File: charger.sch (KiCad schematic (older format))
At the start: 22 parts, among them IC1 BQ51050B

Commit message: Added resistor and capacitor values, footprints and NPNs
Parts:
- C14: footprint (none) -> Capacitors_SMD:C_0402; MPN (none) -> GCM155R71E103KA37D
- C15: footprint (none) -> Capacitors_SMD:C_0402; MPN (none) -> GCM155R71H223KA55D
- C16: footprint (none) -> Capacitors_SMD:C_0402; MPN (none) -> GRT155R61E474KE01D
- C17, C18, C19, C22, C23: footprint (none) -> Capacitors_SMD:C_0402
- C20: footprint (none) -> Capacitors_SMD:C_0603; MPN (none) -> CC0603KRX5R7BB475
- C21: footprint (none) -> Capacitors_SMD:C_0603
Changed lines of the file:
@@
 Battery_voltage
 $Comp
-L +BATT #PWR50
+L +BATT #PWR040
 U 1 1 5AA78F36
 P 8450 2600
-F 0 "#PWR50" H 8450 2450 50  0001 C CNN
+F 0 "#PWR040" H 8450 2450 50  0001 C CNN
 F 1 "+BATT" H 8450 2740 50  0000 C CNN
 F 2 "" H 8450 2600 50  0001 C CNN
@@
 $EndComp
 $Comp
-L GND #PWR51
+L GND #PWR041
 U 1 1 5AA78FC5
 P 8450 3400
-F 0 "#PWR51" H 8450 3150 50  0001 C CNN
+F 0 "#PWR041" H 8450 3150 50  0001 C CNN
 F 1 "GND" H 8450 3250 50  0000 C CNN
 F 2 "" H 8450 3400 50  0001 C CNN
@@
 $EndComp
 $Comp
-L GND #PWR40
+L GND #PWR042
 U 1 1 5AA85C8F
 P 4750 4600
-F 0 "#PWR40" H 4750 4350 50  0001 C CNN
+F 0 "#PWR042" H 4750 4350 50  0001 C CNN
 F 1 "GND" H 4750 4450 50  0000 C CNN
 F 2 "" H 4750 4600 50  0001 C CNN
@@
 $EndComp
 $Comp
-L +BATT #PWR42
+L +BATT #PWR043
 U 1 1 5AA85D44
 P 5100 2800
-F 0 "#PWR42" H 5100 2650 50  0001 C CNN
+F 0 "#PWR043" H 5100 2650 50  0001 C CNN
 F 1 "+BATT" H 5100 2940 50  0000 C CNN
 F 2 "" H 5100 2800 50  0001 C CNN
@@
 $EndComp
 $Comp
-L GND #PWR41
+L GND #PWR044
 U 1 1 5AA86D68
 P 4950 4600
-F 0 "#PWR41" H 4950 4350 50  0001 C CNN
+F 0 "#PWR044" H 4950 4350 50  0001 C CNN
 F 1 "GND" H 4950 4450 50  0000 C CNN
 F 2 "" H 4950 4600 50  0001 C CNN
@@
 $EndComp
 $Comp
-L +BATT #PWR48
+L +BATT #PWR045
 U 1 1 5AA87B72
 P 8450 1150
-F 0 "#PWR48" H 8450 1000 50  0001 C CNN
+F 0 "#PWR045" H 8450 1000 50  0001 C CNN
 F 1 "+BATT" H 8450 1290 50  0000 C CNN
 F 2 "" H 8450 1150 50  0001 C CNN
@@
 F 0 "C23" H 8475 1500 50  0000 L CNN
 F 1 "2u2 6V3" V 8300 1250 50  0000 L CNN
-F 2 "" H 8488 1250 50  0001 C CNN
+F 2 "Capacitors_SMD:C_0402" H 8488 1250 50  0001 C CNN
 F 3 "" H 8450 1400 50  0001 C CNN
 	1    8450 1400
@@
 $EndComp
 $Comp
-L GND #PWR49
+L GND #PWR046
 U 1 1 5AA87C01
 P 8450 1650
-F 0 "#PWR49" H 8450 1400 50  0001 C CNN
+F 0 "#PWR046" H 8450 1400 50  0001 C CNN
 F 1 "GND" H 8450 1500 50  0000 C CNN
 F 2 "" H 8450 1650 50  0001 C CNN
@@
 F 0 "C14" V 3250 2850 50  0000 L CNN
 F 1 "10nF 10V" V 3250 2400 50  0000 L CNN
-F 2 "" H 3188 2650 50  0001 C CNN
+F 2 "Capacitors_SMD:C_0402" H 3188 2650 50  0001 C CNN
 F 3 "" H 3150 2800 50  0001 C CNN
+F 4 "GCM155R71E103KA37D" V 3150 2800 60  0001 C CNN "MPN"
 	1    3150 2800
 	0    -1   -1   0
@@
 F 0 "C19" V 3250 4300 50  0000 L CNN
 F 1 "10nF 10V" V 3250 4550 50  0000 L CNN
-F 2 "" H 3188 4350 50  0001 C CNN
+F 2 "Capacitors_SMD:C_0402" H 3188 4350 50  0001 C CNN
 F 3 "" H 3150 4500 50  0001 C CNN
 	1    3150 4500
@@
 F 0 "C18" V 3250 4050 50  0000 L CNN
 F 1 "22nF 25V" V 3250 4300 50  0000 L CNN
-F 2 "" H 3188 4100 50  0001 C CNN
+F 2 "Capacitors_SMD:C_0402" H 3188 4100 50  0001 C CNN
 F 3 "" H 3150 4250 50  0001 C CNN
 	1    3150 4250
@@
 F 0 "C17" V 3250 3800 50  0000 L CNN
 F 1 "470nF 25V" V 3250 4050 50  0000 L CNN
-F 2 "" H 3188 3850 50  0001 C CNN
+F 2 "Capacitors_SMD:C_0402" H 3188 3850 50  0001 C CNN
 F 3 "" H 3150 4000 50  0001 C CNN
 	1    3150 4000
@@
 F 0 "C16" V 3050 3100 50  0000 L CNN
 F 1 "470nF 25V" V 3050 3350 50  0000 L CNN
-F 2 "" H 3188 3150 50  0001 C CNN
+F 2 "Capacitors_SMD:C_0402" H 3188 3150 50  0001 C CNN
 F 3 "" H 3150 3300 50  0001 C CNN
+F 4 "GRT155R61E474KE01D" V 3150 3300 60  0001 C CNN "MPN"
 	1    3150 3300
 	0    1    1    0
@@
 F 0 "C15" V 3250 3100 50  0000 L CNN
 F 1 "22nF 25V" V 3250 2650 50  0000 L CNN
-F 2 "" H 3188 2900 50  0001 C CNN
+F 2 "Capacitors_SMD:C_0402" H 3188 2900 50  0001 C CNN
 F 3 "" H 3150 3050 50  0001 C CNN
+F 4 "GCM155R71H223KA55D" V 3150 3050 60  0001 C CNN "MPN"
 	1    3150 3050
 	0    -1   -1   0
@@
 Connection ~ 2900 3300
 $Comp
-L VDD #PWR45
+L VDD #PWR047
 U 1 1 5AA8B638
 P 7050 2650
-F 0 "#PWR45" H 7050 2500 50  0001 C CNN
+F 0 "#PWR047" H 7050 2500 50  0001 C CNN
 F 1 "VDD" H 7050 2800 50  0000 C CNN
 F 2 "" H 7050 2650 50  0001 C CNN
@@
 $EndComp
 $Comp
-L GND #PWR46
+L GND #PWR048
 U 1 1 5AB06991
 P 7050 4600
-F 0 "#PWR46" H 7050 4350 50  0001 C CNN
+F 0 "#PWR048" H 7050 4350 50  0001 C CNN
 F 1 "GND" H 7050 4450 50  0000 C CNN
 F 2 "" H 7050 4600 50  0001 C CNN
@@
 F 0 "C20" H 5225 4350 50  0000 L CNN
 F 1 "4u7 16V" V 5400 4100 50  0000 L CNN
-F 2 "" H 5238 4100 50  0001 C CNN
+F 2 "Capacitors_SMD:C_0603" H 5238 4100 50  0001 C CNN
 F 3 "" H 5200 4250 50  0001 C CNN
+F 4 "CC0603KRX5R7BB475" H 5200 4250 60  0001 C CNN "MPN"
 	1    5200 4250
 	1    0    0    -1
@@
 	4650 3600 5550 3600
 $Comp
-L GND #PWR43
+L GND #PWR049
 U 1 1 5AB07537
 P 5200 4600
-F 0 "#PWR43" H 5200 4350 50  0001 C CNN
+F 0 "#PWR049" H 5200 4350 50  0001 C CNN
 F 1 "GND" H 5200 4450 50  0000 C CNN
 F 2 "" H 5200 4600 50  0001 C CNN
@@
 F 0 "C21" H 5575 4350 50  0000 L CNN
 F 1 "4u7 16V" V 5750 4100 50  0000 L CNN
-F 2 "" H 5588 4100 50  0001 C CNN
+F 2 "Capacitors_SMD:C_0603" H 5588 4100 50  0001 C CNN
 F 3 "" H 5550 4250 50  0001 C CNN
 	1    5550 4250
@@
 Connection ~ 5200 3600
 $Comp
-L GND #PWR44
+L GND #PWR050
 U 1 1 5AB15630
 P 5550 4600
-F 0 "#PWR44" H 5550 4350 50  0001 C CNN
+F 0 "#PWR050" H 5550 4350 50  0001 C CNN
 F 1 "GND" H 5550 4450 50  0000 C CNN
 F 2 "" H 5550 4600 50  0001 C CNN
@@
 F 0 "C22" H 7125 1450 50  0000 L CNN
 F 1 "470nF 25V" H 7125 1250 50  0000 L CNN
-F 2 "" H 7138 1200 50  0001 C CNN
+F 2 "Capacitors_SMD:C_0402" H 7138 1200 50  0001 C CNN
 F 3 "" H 7100 1350 50  0001 C CNN
 	1    7100 1350
@@
 $EndComp
 $Comp
-L GND #PWR47
+L GND #PWR051
 U 1 1 5AB160F7
 P 7100 1650
-F 0 "#PWR47" H 7100 1400 50  0001 C CNN
+F 0 "#PWR051" H 7100 1400 50  0001 C CNN
 F 1 "GND" H 7100 1500 50  0000 C CNN
 F 2 "" H 7100 1650 50  0001 C CNN
@@
 	7050 3800 7050 3850
 $Comp
-L PWR_FLAG #FLG1
+L PWR_FLAG #FLG052
 U 1 1 5AB77961
 P 2500 3350
-F 0 "#FLG1" H 2500 3425 50  0001 C CNN
+F 0 "#FLG052" H 2500 3425 50  0001 C CNN
 F 1 "PWR_FLAG" H 2500 3500 50  0000 C CNN
 F 2 "" H 2500 3350 50  0001 C CNN
@@
 $EndComp
 $Comp
-L PWR_FLAG #FLG2
+L PWR_FLAG #FLG053
 U 1 1 5AB77A5F
 P 2900 3700
-F 0 "#FLG2" H 2900 3775 50  0001 C CNN
+F 0 "#FLG053" H 2900 3775 50  0001 C CNN
 F 1 "PWR_FLAG" H 2900 3850 50  0000 C CNN
 F 2 "" H 2900 3700 50  0001 C CNN

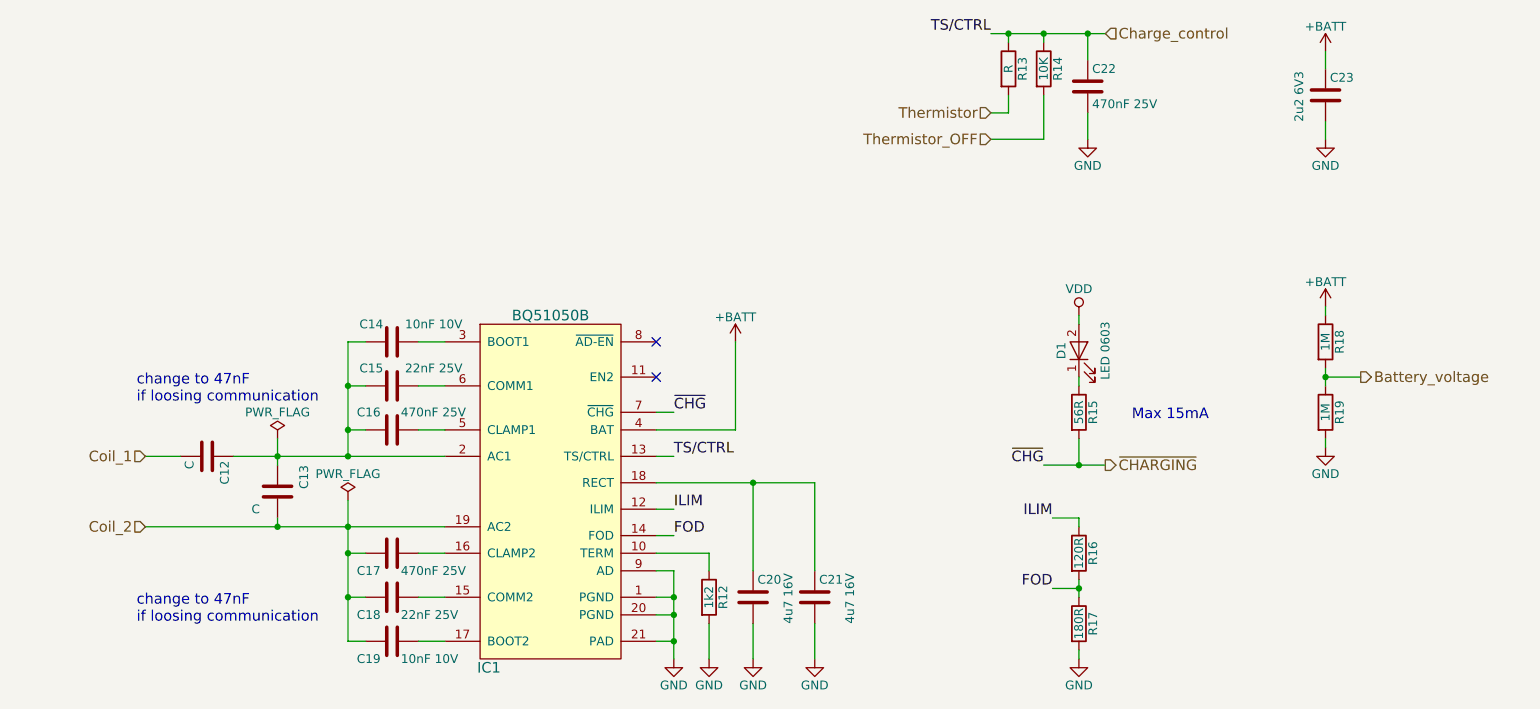
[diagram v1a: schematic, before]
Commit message: Removed boost converter, added output switch
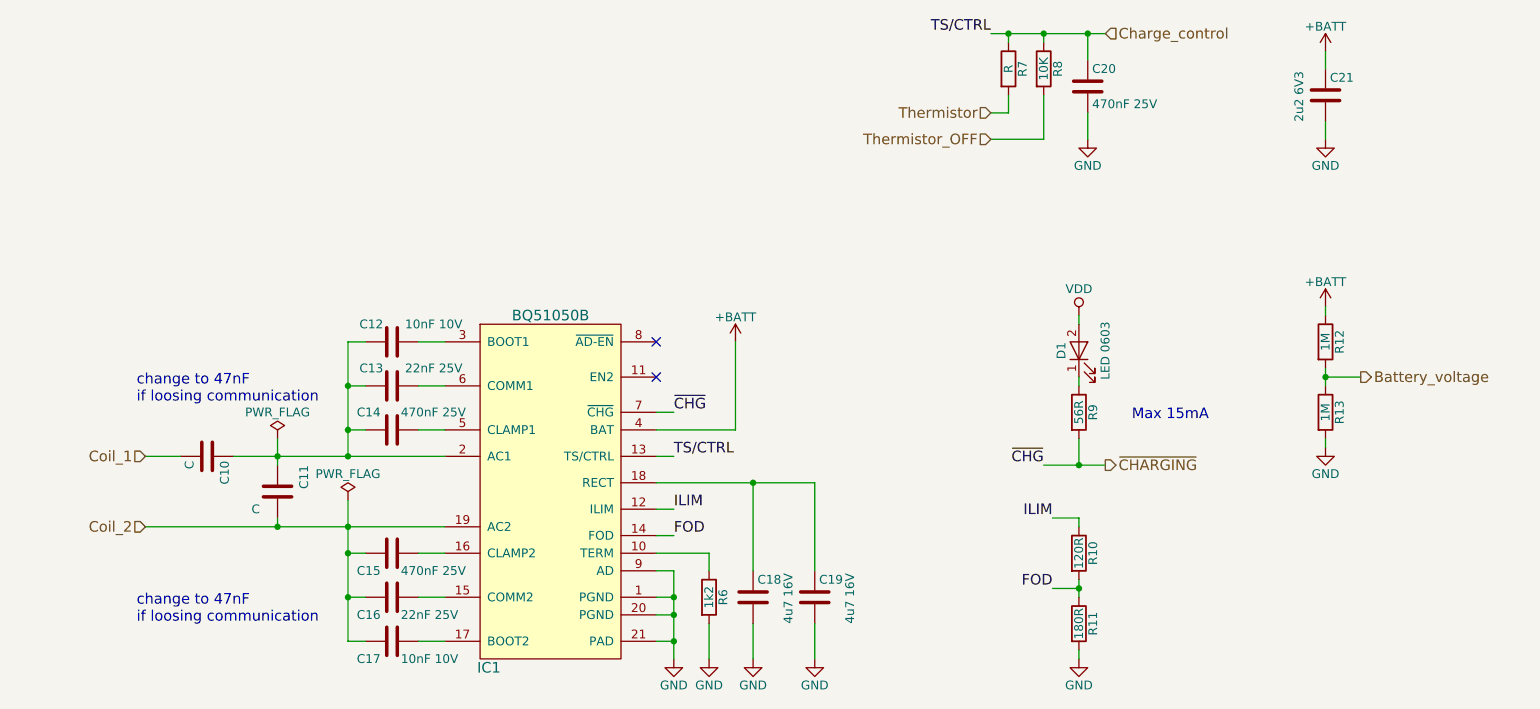
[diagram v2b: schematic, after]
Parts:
- renumbered C12 to C10, C13 to C11, C14 to C12, C15 to C13, C16 to C14, C17 to C15, C18 to C16, C19 to C17, C20 to C18, C21 to C19, C22 to C20, C23 to C21, R16 to R10, R17 to R11, R18 to R12, R19 to R13, R12 to R6, R13 to R7, R14 to R8, R15 to R9
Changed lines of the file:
@@
 LIBS:Transistor
 LIBS:Connector
+LIBS:lakotamm-loadswitch
 LIBS:F3K_Battery_manager-cache
 EELAYER 25 0
@@
 $Descr A4 11693 8268
 encoding utf-8
-Sheet 4 4
+Sheet 3 3
 Title ""
 Date ""
@@
 Battery_voltage
 $Comp
-L +BATT #PWR040
+L +BATT #PWR47
 U 1 1 5AA78F36
 P 8450 2600
-F 0 "#PWR040" H 8450 2450 50  0001 C CNN
+F 0 "#PWR47" H 8450 2450 50  0001 C CNN
 F 1 "+BATT" H 8450 2740 50  0000 C CNN
 F 2 "" H 8450 2600 50  0001 C CNN
@@
 $EndComp
 $Comp
-L R R18
+L R R12
 U 1 1 5AA78F4C
 P 8450 2800
-F 0 "R18" V 8530 2800 50  0000 C CNN
+F 0 "R12" V 8530 2800 50  0000 C CNN
 F 1 "1M" V 8450 2800 50  0000 C CNN
 F 2 "Resistors_SMD:R_0402" V 8380 2800 50  0001 C CNN
@@
 $EndComp
 $Comp
-L R R19
+L R R13
 U 1 1 5AA78F86
 P 8450 3200
-F 0 "R19" V 8530 3200 50  0000 C CNN
+F 0 "R13" V 8530 3200 50  0000 C CNN
 F 1 "1M" V 8450 3200 50  0000 C CNN
 F 2 "Resistors_SMD:R_0402" V 8380 3200 50  0001 C CNN
@@
 $EndComp
 $Comp
-L GND #PWR041
+L GND #PWR48
 U 1 1 5AA78FC5
 P 8450 3400
-F 0 "#PWR041" H 8450 3150 50  0001 C CNN
+F 0 "#PWR48" H 8450 3150 50  0001 C CNN
 F 1 "GND" H 8450 3250 50  0000 C CNN
 F 2 "" H 8450 3400 50  0001 C CNN
@@
 $EndComp
 $Comp
-L GND #PWR042
+L GND #PWR37
 U 1 1 5AA85C8F
 P 4750 4600
-F 0 "#PWR042" H 4750 4350 50  0001 C CNN
+F 0 "#PWR37" H 4750 4350 50  0001 C CNN
 F 1 "GND" H 4750 4450 50  0000 C CNN
 F 2 "" H 4750 4600 50  0001 C CNN
@@
 $EndComp
 $Comp
-L +BATT #PWR043
+L +BATT #PWR39
 U 1 1 5AA85D44
 P 5100 2800
-F 0 "#PWR043" H 5100 2650 50  0001 C CNN
+F 0 "#PWR39" H 5100 2650 50  0001 C CNN
 F 1 "+BATT" H 5100 2940 50  0000 C CNN
 F 2 "" H 5100 2800 50  0001 C CNN
@@
 NoConn ~ 4650 2800
 $Comp
-L R R15
+L R R9
 U 1 1 5AA85E7B
 P 7050 3200
-F 0 "R15" V 7130 3200 50  0000 C CNN
+F 0 "R9" V 7130 3200 50  0000 C CNN
 F 1 "56R" V 7050 3200 50  0000 C CNN
 F 2 "Resistors_SMD:R_0402" V 6980 3200 50  0001 C CNN
@@
 ~CHARGING
 $Comp
-L R R12
+L R R6
 U 1 1 5AA86C77
 P 4950 4250
-F 0 "R12" V 5030 4250 50  0000 C CNN
+F 0 "R6" V 5030 4250 50  0000 C CNN
 F 1 "1k2" V 4950 4250 50  0000 C CNN
 F 2 "Resistors_SMD:R_0402" V 4880 4250 50  0001 C CNN
@@
 $EndComp
 $Comp
-L GND #PWR044
+L GND #PWR38
 U 1 1 5AA86D68
 P 4950 4600
-F 0 "#PWR044" H 4950 4350 50  0001 C CNN
+F 0 "#PWR38" H 4950 4350 50  0001 C CNN
 F 1 "GND" H 4950 4450 50  0000 C CNN
 F 2 "" H 4950 4600 50  0001 C CNN
@@
 $EndComp
 $Comp
-L +BATT #PWR045
+L +BATT #PWR45
 U 1 1 5AA87B72
 P 8450 1150
-F 0 "#PWR045" H 8450 1000 50  0001 C CNN
+F 0 "#PWR45" H 8450 1000 50  0001 C CNN
 F 1 "+BATT" H 8450 1290 50  0000 C CNN
 F 2 "" H 8450 1150 50  0001 C CNN
@@
 $EndComp
 $Comp
-L C C23
+L C C21
 U 1 1 5AA87B8B
 P 8450 1400
-F 0 "C23" H 8475 1500 50  0000 L CNN
+F 0 "C21" H 8475 1500 50  0000 L CNN
 F 1 "2u2 6V3" V 8300 1250 50  0000 L CNN
 F 2 "Capacitors_SMD:C_0402" H 8488 1250 50  0001 C CNN
@@
 $EndComp
 $Comp
-L GND #PWR046
+L GND #PWR46
 U 1 1 5AA87C01
 P 8450 1650
-F 0 "#PWR046" H 8450 1400 50  0001 C CNN
+F 0 "#PWR46" H 8450 1400 50  0001 C CNN
 F 1 "GND" H 8450 1500 50  0000 C CNN
 F 2 "" H 8450 1650 50  0001 C CNN
@@
 $EndComp
 $Comp
-L C C14
+L C C12
 U 1 1 5AA87D3B
 P 3150 2800
-F 0 "C14" V 3250 2850 50  0000 L CNN
+F 0 "C12" V 3250 2850 50  0000 L CNN
 F 1 "10nF 10V" V 3250 2400 50  0000 L CNN
 F 2 "Capacitors_SMD:C_0402" H 3188 2650 50  0001 C CNN
@@
 $EndComp
 $Comp
-L C C19
+L C C17
 U 1 1 5AA87DF5
 P 3150 4500
-F 0 "C19" V 3250 4300 50  0000 L CNN
+F 0 "C17" V 3250 4300 50  0000 L CNN
 F 1 "10nF 10V" V 3250 4550 50  0000 L CNN
 F 2 "Capacitors_SMD:C_0402" H 3188 4350 50  0001 C CNN
@@
 $EndComp
 $Comp
-L C C18
+L C C16
 U 1 1 5AA882B8
 P 3150 4250
-F 0 "C18" V 3250 4050 50  0000 L CNN
+F 0 "C16" V 3250 4050 50  0000 L CNN
 F 1 "22nF 25V" V 3250 4300 50  0000 L CNN
 F 2 "Capacitors_SMD:C_0402" H 3188 4100 50  0001 C CNN
@@
 change to 47nF \nif loosing communication
 $Comp
-L C C17
+L C C15
 U 1 1 5AA8A27D
 P 3150 4000
-F 0 "C17" V 3250 3800 50  0000 L CNN
+F 0 "C15" V 3250 3800 50  0000 L CNN
 F 1 "470nF 25V" V 3250 4050 50  0000 L CNN
 F 2 "Capacitors_SMD:C_0402" H 3188 3850 50  0001 C CNN
@@
 $EndComp
 $Comp
-L C C16
+L C C14
 U 1 1 5AA8A4C2
 P 3150 3300
-F 0 "C16" V 3050 3100 50  0000 L CNN
+F 0 "C14" V 3050 3100 50  0000 L CNN
 F 1 "470nF 25V" V 3050 3350 50  0000 L CNN
 F 2 "Capacitors_SMD:C_0402" H 3188 3150 50  0001 C CNN
@@
 $EndComp
 $Comp
-L C C15
+L C C13
 U 1 1 5AA88198
 P 3150 3050
-F 0 "C15" V 3250 3100 50  0000 L CNN
+F 0 "C13" V 3250 3100 50  0000 L CNN
 F 1 "22nF 25V" V 3250 2650 50  0000 L CNN
 F 2 "Capacitors_SMD:C_0402" H 3188 2900 50  0001 C CNN
@@
 Connection ~ 2900 3300
 $Comp
-L VDD #PWR047
+L VDD #PWR42
 U 1 1 5AA8B638
 P 7050 2650
-F 0 "#PWR047" H 7050 2500 50  0001 C CNN
+F 0 "#PWR42" H 7050 2500 50  0001 C CNN
 F 1 "VDD" H 7050 2800 50  0000 C CNN
 F 2 "" H 7050 2650 50  0001 C CNN
@@
 Max 15mA\n
 $Comp
-L C C13
+L C C11
 U 1 1 5AB055C0
 P 2500 3650
-F 0 "C13" V 2350 3500 50  0000 L CNN
+F 0 "C11" V 2350 3500 50  0000 L CNN
 F 1 "C" H 2600 3750 50  0000 L CNN
 F 2 "" H 2538 3500 50  0001 C CNN
@@
 $EndComp
 $Comp
-L C C12
+L C C10
 U 1 1 5AB0567E
 P 2100 3450
-F 0 "C12" H 2125 3550 50  0000 L CNN
+F 0 "C10" H 2125 3550 50  0000 L CNN
 F 1 "C" H 2125 3350 50  0000 L CNN
 F 2 "" H 2138 3300 50  0001 C CNN
@@
 	2900 3700 2900 4500
 $Comp
-L R R17
+L R R11
 U 1 1 5AB0687F
 P 7050 4400
-F 0 "R17" V 7130 4400 50  0000 C CNN
+F 0 "R11" V 7130 4400 50  0000 C CNN
 F 1 "180R" V 7050 4400 50  0000 C CNN
 F 2 "Resistors_SMD:R_0402" V 6980 4400 50  0001 C CNN
@@
 $EndComp
 $Comp
-L GND #PWR048
+L GND #PWR43
 U 1 1 5AB06991
 P 7050 4600
-F 0 "#PWR048" H 7050 4350 50  0001 C CNN
+F 0 "#PWR43" H 7050 4350 50  0001 C CNN
 F 1 "GND" H 7050 4450 50  0000 C CNN
 F 2 "" H 7050 4600 50  0001 C CNN
@@
 	4650 3450 4750 3450
 $Comp
-L C C20
+L C C18
 U 1 1 5AB0745B
 P 5200 4250
-F 0 "C20" H 5225 4350 50  0000 L CNN
+F 0 "C18" H 5225 4350 50  0000 L CNN
 F 1 "4u7 16V" V 5400 4100 50  0000 L CNN
 F 2 "Capacitors_SMD:C_0603" H 5238 4100 50  0001 C CNN
@@
 	4650 3600 5550 3600
 $Comp
-L GND #PWR049
+L GND #PWR40
 U 1 1 5AB07537
 P 5200 4600
-F 0 "#PWR049" H 5200 4350 50  0001 C CNN
+F 0 "#PWR40" H 5200 4350 50  0001 C CNN
 F 1 "GND" H 5200 4450 50  0000 C CNN
 F 2 "" H 5200 4600 50  0001 C CNN
@@
 Thermistor
 $Comp
-L C C21
+L C C19
 U 1 1 5AB15596
 P 5550 4250
-F 0 "C21" H 5575 4350 50  0000 L CNN
+F 0 "C19" H 5575 4350 50  0000 L CNN
 F 1 "4u7 16V" V 5750 4100 50  0000 L CNN
 F 2 "Capacitors_SMD:C_0603" H 5588 4100 50  0001 C CNN
@@
 Connection ~ 5200 3600
 $Comp
-L GND #PWR050
+L GND #PWR41
 U 1 1 5AB15630
 P 5550 4600
-F 0 "#PWR050" H 5550 4350 50  0001 C CNN
+F 0 "#PWR41" H 5550 4350 50  0001 C CNN
 F 1 "GND" H 5550 4450 50  0000 C CNN
 F 2 "" H 5550 4600 50  0001 C CNN
@@
 	5550 4400 5550 4600
 $Comp
-L R R13
+L R R7
 U 1 1 5AB15ADC
 P 6650 1250
-F 0 "R13" V 6730 1250 50  0000 C CNN
+F 0 "R7" V 6730 1250 50  0000 C CNN
 F 1 "R" V 6650 1250 50  0000 C CNN
 F 2 "Resistors_SMD:R_0402" V 6580 1250 50  0001 C CNN
@@
 	6650 1500 6650 1400
 $Comp
-L C C22
+L C C20
 U 1 1 5AB15F72
 P 7100 1350
-F 0 "C22" H 7125 1450 50  0000 L CNN
+F 0 "C20" H 7125 1450 50  0000 L CNN
 F 1 "470nF 25V" H 7125 1250 50  0000 L CNN
 F 2 "Capacitors_SMD:C_0402" H 7138 1200 50  0001 C CNN
@@
 $EndComp
 $Comp
-L GND #PWR051
+L GND #PWR44
 U 1 1 5AB160F7
 P 7100 1650
-F 0 "#PWR051" H 7100 1400 50  0001 C CNN
+F 0 "#PWR44" H 7100 1400 50  0001 C CNN
 F 1 "GND" H 7100 1500 50  0000 C CNN
 F 2 "" H 7100 1650 50  0001 C CNN
@@
 	7100 1500 7100 1650
 $Comp
-L R R14
+L R R8
 U 1 1 5AB17BEE
 P 6850 1250
-F 0 "R14" V 6930 1250 50  0000 C CNN
+F 0 "R8" V 6930 1250 50  0000 C CNN
 F 1 "10K" V 6850 1250 50  0000 C CNN
 F 2 "Resistors_SMD:R_0402" V 6780 1250 50  0001 C CNN
@@
 	7050 4150 7050 4250
 $Comp
-L R R16
+L R R10
 U 1 1 5AB580B7
 P 7050 4000
-F 0 "R16" V 7130 4000 50  0000 C CNN
+F 0 "R10" V 7130 4000 50  0000 C CNN
 F 1 "120R" V 7050 4000 50  0000 C CNN
 F 2 "Resistors_SMD:R_0402" V 6980 4000 50  0001 C CNN
@@
 	7050 3800 7050 3850
 $Comp
-L PWR_FLAG #FLG052
+L PWR_FLAG #FLG1
 U 1 1 5AB77961
 P 2500 3350
-F 0 "#FLG052" H 2500 3425 50  0001 C CNN
+F 0 "#FLG1" H 2500 3425 50  0001 C CNN
 F 1 "PWR_FLAG" H 2500 3500 50  0000 C CNN
 F 2 "" H 2500 3350 50  0001 C CNN
@@
 $EndComp
 $Comp
-L PWR_FLAG #FLG053
+L PWR_FLAG #FLG2
 U 1 1 5AB77A5F
 P 2900 3700
-F 0 "#FLG053" H 2900 3775 50  0001 C CNN
+F 0 "#FLG2" H 2900 3775 50  0001 C CNN
 F 1 "PWR_FLAG" H 2900 3850 50  0000 C CNN
 F 2 "" H 2900 3700 50  0001 C CNN
